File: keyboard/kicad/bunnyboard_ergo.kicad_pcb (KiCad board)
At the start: 2 copper layers, 236.5 x 97.1 mm, 57 parts, among them U2 Pico

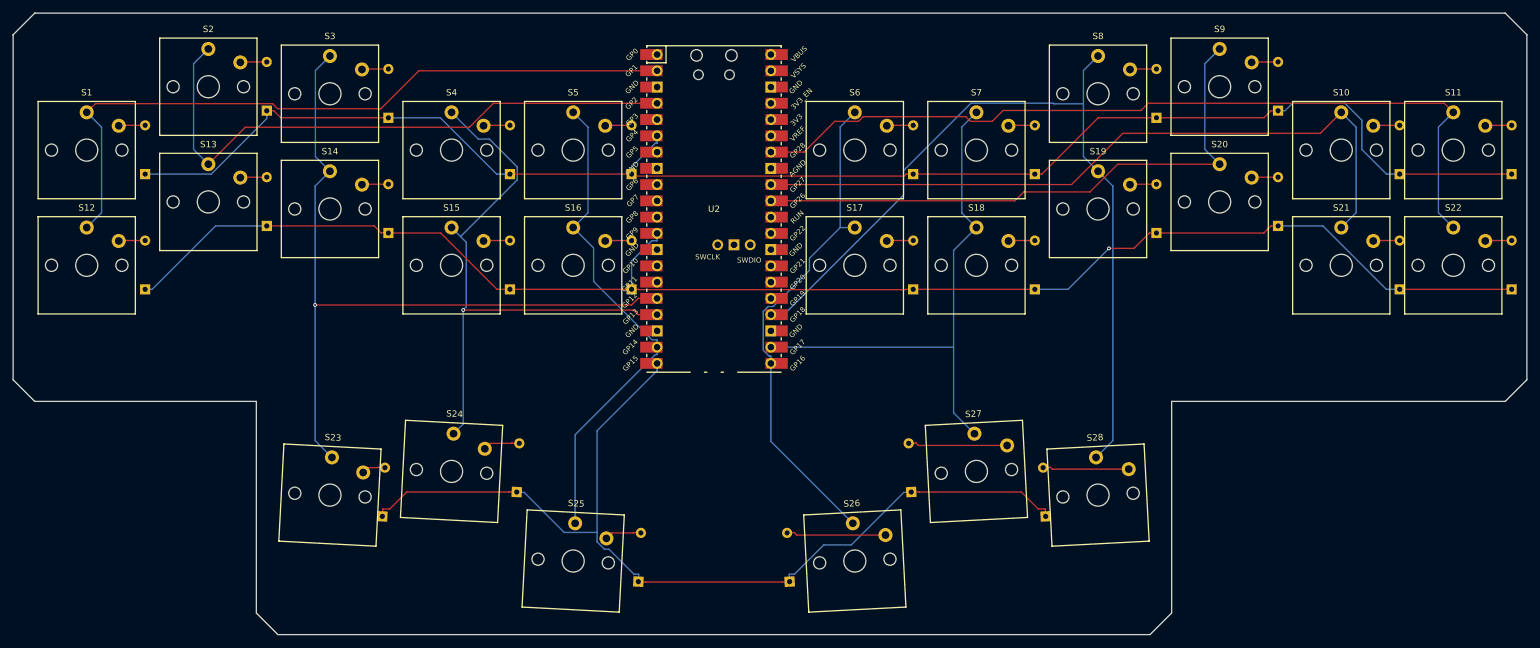
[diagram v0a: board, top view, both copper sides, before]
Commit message: ergo: Daumenwinkel auf 6 Grad (nach innen)
- THUMB_ROT 3 -> 6. Richtung unveraendert (links -6, rechts +6).
- Nur S23-S28 gedreht; S1-S22 und Pico bleiben bei 0. PCB-Geometrie
  (Umriss, Pico, Finger) unangetastet.
- Kappenluecke S23-S24 sinkt von 0.94 auf 0.13 mm (Kappen-BBox 19.23 mm
  bei 19.36 mm Mittenabstand). Ab 8 Grad ueberlappen die Kappen.
- 283 Tracks, 0 DRC, 0 unconnected.
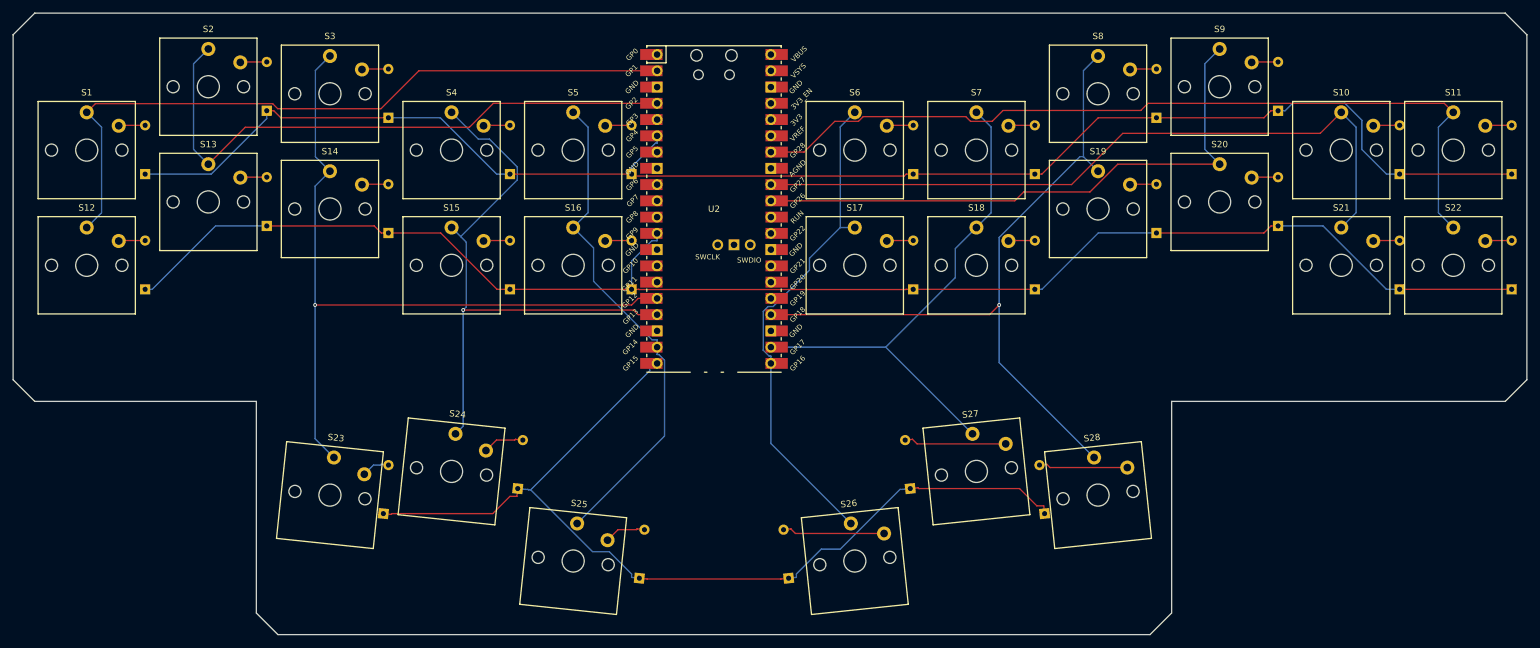
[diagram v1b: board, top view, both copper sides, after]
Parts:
- moved D24 0.56 mm to (-30.7, 43.7), turned to 84 degrees
- moved D25 0.56 mm to (-11.7, 57.7), turned to 84 degrees
- moved D26 0.56 mm to (11.7, 57.7), turned to 96 degrees
- moved D27 0.56 mm to (30.7, 43.7), turned to 96 degrees
- moved D23 0.46 mm to (-51.7, 47.6), turned to 84 degrees
- moved D28 0.46 mm to (51.7, 47.6), turned to 96 degrees
- turned S23 to -6 degrees
- turned S24 to -6 degrees
- turned S25 to -6 degrees
- turned S26 to 6 degrees
- turned S27 to 6 degrees
- turned S28 to 6 degrees
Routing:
- net Column 7: track 131.4 -> 115.1 mm, vias 0 -> 1
- net Row 2: track 152.3 -> 148.5 mm
- net Column 6: track 83.5 -> 81.6 mm
- net Column 4: track 77.5 -> 78.3 mm
- net Net-(D24-A): track 5.77 -> 6.50 mm
- net Net-(D25-A): track 5.77 -> 6.50 mm
- net Net-(D23-A): track 3.73 -> 4.42 mm
- net Row 1: vias 1 -> 0

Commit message: ergo: Daumen 9 Grad in V-Form (links +9, rechts -9)
- Richtung gedreht: links +THUMB_ROT, rechts -THUMB_ROT. Die Kappen kippen
  damit zur Mitte nach oben, es entsteht ein V zwischen den Daumen.
  Vorzeichen ueber die Oberkanten-Normale im SVG-Koordinatensystem
  hergeleitet: n = (sin a, -cos a); links muss nach rechts kippen (a>0),
  rechts nach links (a<0). Gegenprobe Pad-Achse: links 13.78, rechts 31.78.
- Winkel 9 Grad (nicht 6): 3 Grad + 6 Grad weiter nach innen.
- Dioden-Offsets der Randtasten S23/S28 von -8 auf +10 umgestellt, weil sich
  mit der neuen Drehrichtung die Richtung zur Cluster-Mitte umkehrt
  (DRC hole_clearance an D23/D28).
- Nur S23-S28 gedreht; S1-S22 und Pico bleiben bei 0. Umriss/Pico unveraendert.
- 274 Tracks, 0 DRC, 0 unconnected.
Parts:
- moved D24 2.79 mm to (-31.7, 46.3), turned to 99 degrees
- moved D27 2.79 mm to (31.7, 46.3), turned to 81 degrees
- moved D25 2.79 mm to (-12.7, 60.3), turned to 99 degrees
- moved D26 2.79 mm to (12.7, 60.3), turned to 81 degrees
- moved D23 2.56 mm to (-50.7, 50.0), turned to 99 degrees
- moved D28 2.56 mm to (50.7, 50.0), turned to 81 degrees
- turned S23 to 9 degrees
- turned S24 to 9 degrees
- turned S25 to 9 degrees
- turned S26 to -9 degrees
- turned S27 to -9 degrees
- turned S28 to -9 degrees
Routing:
- net Column 6: track 81.6 -> 92.4 mm
- net Column 7: track 115.1 -> 118.7 mm
- net Row 1: track 240.8 -> 242.1 mm
- net Row 2: track 148.5 -> 149.8 mm
- net Net-(D24-A): track 6.50 -> 5.21 mm
- net Net-(D25-A): track 6.50 -> 5.21 mm
- net Net-(D27-A): track 16.0 -> 14.8 mm
- net Net-(D26-A): track 16.0 -> 14.8 mm
- net Net-(D28-A): track 13.9 -> 14.8 mm
- net Net-(D23-A): track 4.42 -> 5.21 mm
- net Column 5: track 78.7 -> 79.4 mm
- net Column 2: track 120.7 -> 120.1 mm

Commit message: ergo: Daumenwinkel zurueck auf 3 Grad, V-Form beibehalten
- THUMB_ROT 9 -> 3. Richtung unveraendert: links +3 (Kappe kippt nach
  rechtsoben), rechts -3 (nach linksoben) -> V zwischen den Daumen.
- Dioden-Offsets bleiben bei +-10.0 (zur Cluster-Mitte).
- Nur S23-S28 gedreht; S1-S22 und Pico bei 0. Umriss/Pico unveraendert,
  Board 236.6 x 97.2 mm.
- 282 Tracks, 0 DRC, 0 unconnected.
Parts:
- moved D24 1.12 mm to (-31.2, 45.3), turned to 93 degrees
- moved D27 1.12 mm to (31.2, 45.3), turned to 87 degrees
- moved D25 1.12 mm to (-12.2, 59.3), turned to 93 degrees
- moved D26 1.12 mm to (12.2, 59.3), turned to 87 degrees
- moved D23 1.12 mm to (-50.2, 49.0), turned to 93 degrees
- moved D28 1.12 mm to (50.2, 49.0), turned to 87 degrees
- turned S23 to 3 degrees
- turned S24 to 3 degrees
- turned S25 to 3 degrees
- turned S26 to -3 degrees
- turned S27 to -3 degrees
- turned S28 to -3 degrees
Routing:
- net Row 2: track 149.8 -> 144.3 mm
- net Column 4: track 78.1 -> 78.7 mm

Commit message: ergo: Daumenrichtung umgedreht, 3 Grad (links -3, rechts +3)
- Vorzeichen getauscht: links -THUMB_ROT, rechts +THUMB_ROT. Die
  Kappen-Oberkante kippt jetzt von der Mitte nach aussen.
- Winkel bleibt 3 Grad.
- Gegenprobe Pad-Achse: links -3 -> 25.78, rechts +3 -> 19.78 (gespiegelt).
- Dioden-Offsets +-10.0 unveraendert.
- Nur S23-S28 gedreht; S1-S22 und Pico bei 0. Umriss/Pico unveraendert,
  Board 236.6 x 97.2 mm.
- 290 Tracks, 0 DRC, 0 unconnected.
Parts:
- moved D23 1.12 mm to (-49.8, 47.9), turned to 87 degrees
- moved D24 1.12 mm to (-30.8, 44.2), turned to 87 degrees
- moved D25 1.12 mm to (-11.8, 58.2), turned to 87 degrees
- moved D26 1.12 mm to (11.8, 58.2), turned to 93 degrees
- moved D27 1.12 mm to (30.8, 44.2), turned to 93 degrees
- moved D28 1.12 mm to (49.8, 47.9), turned to 93 degrees
- turned S23 to -3 degrees
- turned S24 to -3 degrees
- turned S25 to -3 degrees
- turned S26 to 3 degrees
- turned S27 to 3 degrees
- turned S28 to 3 degrees
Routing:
- net Column 7: track 118.4 -> 131.4 mm, vias 1 -> 0
- net Column 6: track 91.9 -> 83.5 mm
- net Row 2: track 144.3 -> 148.2 mm
- net Row 1: track 242.1 -> 240.8 mm, vias 0 -> 1
- net Column 4: track 78.7 -> 77.5 mm
- net Net-(D28-A): track 14.7 -> 15.5 mm
- net Net-(D23-A): track 4.92 -> 5.77 mm
- net Net-(D25-A): track 4.92 -> 5.77 mm
- net Net-(D26-A): track 14.7 -> 15.5 mm
- net Net-(D27-A): track 14.7 -> 15.5 mm
- net Net-(D24-A): track 4.92 -> 5.77 mm
